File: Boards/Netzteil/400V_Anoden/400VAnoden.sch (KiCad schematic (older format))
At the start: 48 parts, among them P1 Drossel, P2 320V_AC, P3 Stabi, P4 133V_AC, P5 Stabi, P6 Trafo, P7 Trafo, P8 Relay, Q1 2SC2979

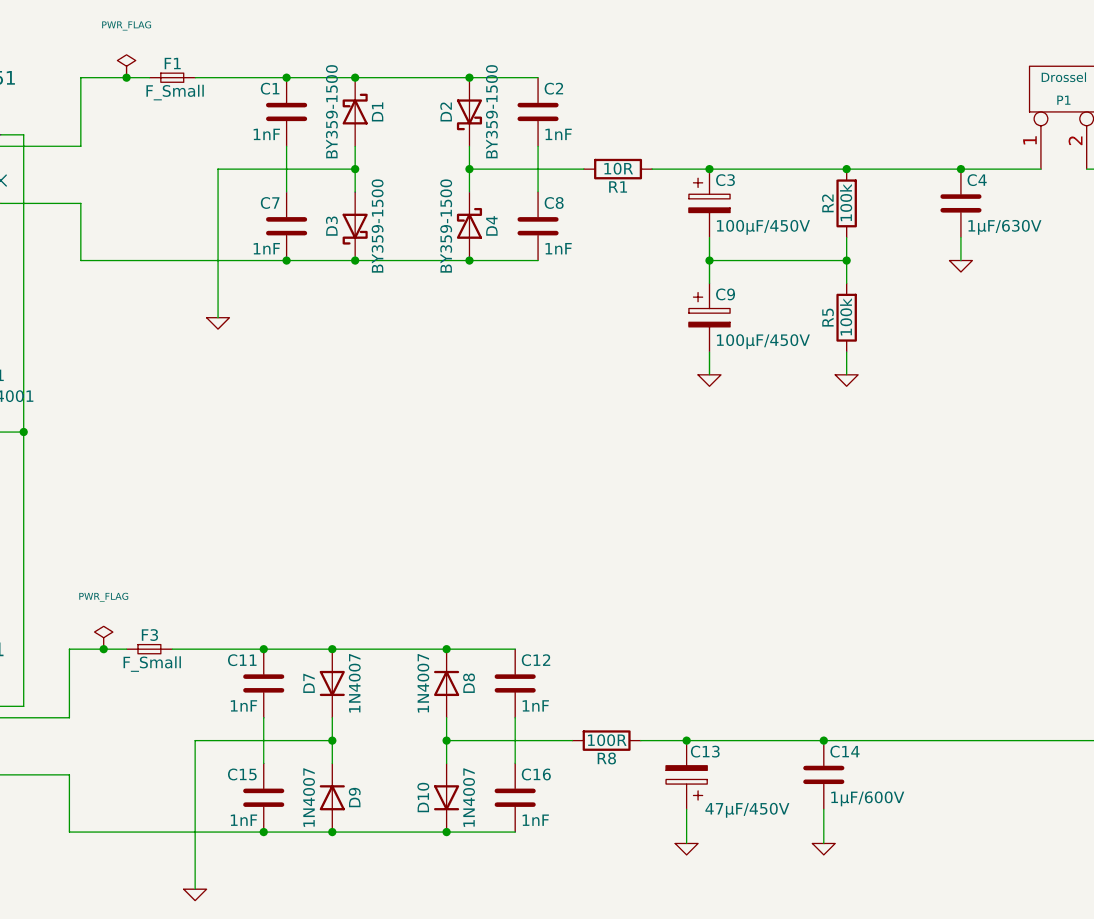
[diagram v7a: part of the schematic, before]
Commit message: 6,3V und 12V auf einer Platine zusammengefasst
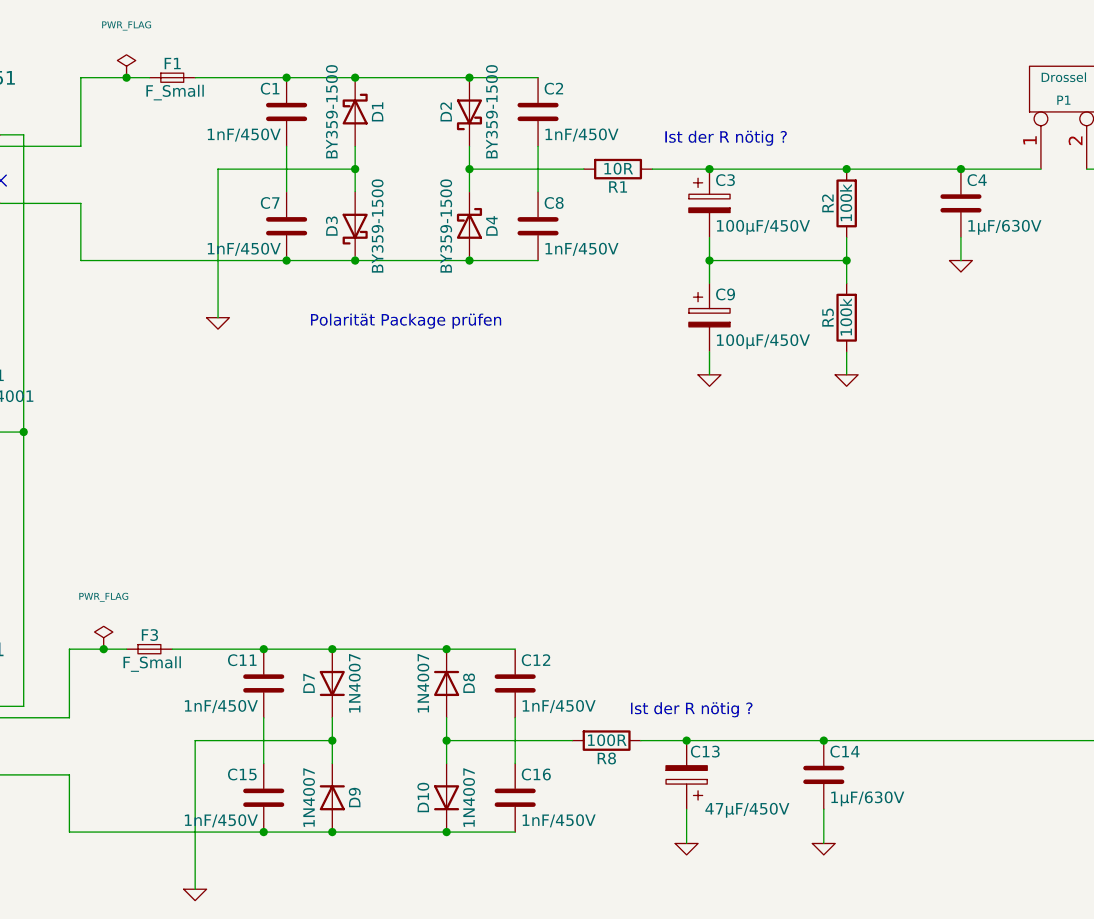
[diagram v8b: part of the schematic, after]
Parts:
- C1, C11, C12, C15, C16, C2, C7, C8: value 1nF -> 1nF/450V; footprint Capacitor_THT:C_Rect_L18.0mm_W5.0mm_P15.00mm_FKS3_FKP3 -> Capacitor_THT:C_Rect_L10.0mm_W4.0mm_P7.50mm_FKS3_FKP3
- C14: value 1µF/600V -> 1µF/630V; footprint Capacitor_THT:C_Rect_L41.5mm_W20.0mm_P37.50mm_MKS4 -> Capacitor_THT:C_Rect_L31.5mm_W11.0mm_P27.50mm_MKS4
- C3: footprint Capacitor_THT:CP_Radial_D22.0mm_P10.00mm_SnapIn -> Capacitor_THT:CP_Radial_D18.0mm_P7.50mm
- C4, C5: footprint Capacitor_THT:C_Rect_L41.5mm_W20.0mm_P37.50mm_MKS4 -> Capacitor_THT:C_Rect_L31.5mm_W11.0mm_P27.50mm_MKS4
- Q1: footprint Package_TO_SOT_THT:TO-220-3_Horizontal_TabDown -> Package_TO_SOT_THT:TO-218-3_Vertical
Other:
- note added: "Ist der R nötig ?"
- note added: "Polarität Package prüfen"
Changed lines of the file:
@@
 EESchema Schematic File Version 4
-LIBS:400VAnoden-cache
 EELAYER 30 0
 EELAYER END
@@
 F 0 "C3" H 5125 2750 50  0000 L CNN
 F 1 "100µF/450V" H 5125 2550 50  0000 L CNN
-F 2 "Capacitor_THT:CP_Radial_D22.0mm_P10.00mm_SnapIn" H 5138 2500 30  0001 C CNN
+F 2 "Capacitor_THT:CP_Radial_D18.0mm_P7.50mm" H 5138 2500 30  0001 C CNN
 F 3 "" H 5100 2650 60  0000 C CNN
 	1    5100 2650
@@
 F 0 "C4" H 6225 2750 50  0000 L CNN
 F 1 "1µF/630V" H 6225 2550 50  0000 L CNN
-F 2 "Capacitor_THT:C_Rect_L41.5mm_W20.0mm_P37.50mm_MKS4" H 6238 2500 30  0001 C CNN
+F 2 "Capacitor_THT:C_Rect_L31.5mm_W11.0mm_P27.50mm_MKS4" H 6238 2500 30  0001 C CNN
 F 3 "" H 6200 2650 60  0000 C CNN
 	1    6200 2650
@@
 F 0 "C5" H 7025 2750 50  0000 L CNN
 F 1 "1µF/630V" H 7025 2550 50  0000 L CNN
-F 2 "Capacitor_THT:C_Rect_L41.5mm_W20.0mm_P37.50mm_MKS4" H 7038 2500 30  0001 C CNN
+F 2 "Capacitor_THT:C_Rect_L31.5mm_W11.0mm_P27.50mm_MKS4" H 7038 2500 30  0001 C CNN
 F 3 "" H 7000 2650 60  0000 C CNN
 	1    7000 2650
@@
 F 0 "Q1" H 9450 2950 50  0000 R CNN
 F 1 "2SC2979" H 9750 2850 50  0000 R CNN
-F 2 "Package_TO_SOT_THT:TO-220-3_Horizontal_TabDown" H 9350 3000 29  0001 C CNN
+F 2 "Package_TO_SOT_THT:TO-218-3_Vertical" H 9350 3000 29  0001 C CNN
 F 3 "" H 9150 2900 60  0000 C CNN
 	1    9150 2900
@@
 P 5600 5150
 F 0 "C14" H 5625 5250 50  0000 L CNN
-F 1 "1µF/600V" H 5625 5050 50  0000 L CNN
-F 2 "Capacitor_THT:C_Rect_L41.5mm_W20.0mm_P37.50mm_MKS4" H 5638 5000 30  0001 C CNN
+F 1 "1µF/630V" H 5625 5050 50  0000 L CNN
+F 2 "Capacitor_THT:C_Rect_L31.5mm_W11.0mm_P27.50mm_MKS4" H 5638 5000 30  0001 C CNN
 F 3 "" H 5600 5150 60  0000 C CNN
 	1    5600 5150
@@
 P 3250 2250
 F 0 "C1" H 3275 2350 50  0000 L CNN
-F 1 "1nF" H 3275 2150 50  0000 L CNN
-F 2 "Capacitor_THT:C_Rect_L18.0mm_W5.0mm_P15.00mm_FKS3_FKP3" H 3288 2100 30  0001 C CNN
+F 1 "1nF/450V" H 3275 2150 50  0000 L CNN
+F 2 "Capacitor_THT:C_Rect_L10.0mm_W4.0mm_P7.50mm_FKS3_FKP3" H 3288 2100 30  0001 C CNN
 F 3 "" H 3250 2250 60  0000 C CNN
 	1    3250 2250
@@
 P 3250 2750
 F 0 "C7" H 3275 2850 50  0000 L CNN
-F 1 "1nF" H 3275 2650 50  0000 L CNN
-F 2 "Capacitor_THT:C_Rect_L18.0mm_W5.0mm_P15.00mm_FKS3_FKP3" H 3288 2600 30  0001 C CNN
+F 1 "1nF/450V" H 3275 2650 50  0000 L CNN
+F 2 "Capacitor_THT:C_Rect_L10.0mm_W4.0mm_P7.50mm_FKS3_FKP3" H 3288 2600 30  0001 C CNN
 F 3 "" H 3250 2750 60  0000 C CNN
 	1    3250 2750
@@
 P 4350 2250
 F 0 "C2" H 4375 2350 50  0000 L CNN
-F 1 "1nF" H 4375 2150 50  0000 L CNN
-F 2 "Capacitor_THT:C_Rect_L18.0mm_W5.0mm_P15.00mm_FKS3_FKP3" H 4388 2100 30  0001 C CNN
+F 1 "1nF/450V" H 4375 2150 50  0000 L CNN
+F 2 "Capacitor_THT:C_Rect_L10.0mm_W4.0mm_P7.50mm_FKS3_FKP3" H 4388 2100 30  0001 C CNN
 F 3 "" H 4350 2250 60  0000 C CNN
 	1    4350 2250
@@
 P 4350 2750
 F 0 "C8" H 4375 2850 50  0000 L CNN
-F 1 "1nF" H 4375 2650 50  0000 L CNN
-F 2 "Capacitor_THT:C_Rect_L18.0mm_W5.0mm_P15.00mm_FKS3_FKP3" H 4388 2600 30  0001 C CNN
+F 1 "1nF/450V" H 4375 2650 50  0000 L CNN
+F 2 "Capacitor_THT:C_Rect_L10.0mm_W4.0mm_P7.50mm_FKS3_FKP3" H 4388 2600 30  0001 C CNN
 F 3 "" H 4350 2750 60  0000 C CNN
 	1    4350 2750
@@
 P 3150 4750
 F 0 "C11" H 3175 4850 50  0000 L CNN
-F 1 "1nF" H 3175 4650 50  0000 L CNN
-F 2 "Capacitor_THT:C_Rect_L18.0mm_W5.0mm_P15.00mm_FKS3_FKP3" H 3188 4600 30  0001 C CNN
+F 1 "1nF/450V" H 3175 4650 50  0000 L CNN
+F 2 "Capacitor_THT:C_Rect_L10.0mm_W4.0mm_P7.50mm_FKS3_FKP3" H 3188 4600 30  0001 C CNN
 F 3 "" H 3150 4750 60  0000 C CNN
 	1    3150 4750
@@
 P 3150 5250
 F 0 "C15" H 3175 5350 50  0000 L CNN
-F 1 "1nF" H 3175 5150 50  0000 L CNN
-F 2 "Capacitor_THT:C_Rect_L18.0mm_W5.0mm_P15.00mm_FKS3_FKP3" H 3188 5100 30  0001 C CNN
+F 1 "1nF/450V" H 3175 5150 50  0000 L CNN
+F 2 "Capacitor_THT:C_Rect_L10.0mm_W4.0mm_P7.50mm_FKS3_FKP3" H 3188 5100 30  0001 C CNN
 F 3 "" H 3150 5250 60  0000 C CNN
 	1    3150 5250
@@
 P 4250 4750
 F 0 "C12" H 4275 4850 50  0000 L CNN
-F 1 "1nF" H 4275 4650 50  0000 L CNN
-F 2 "Capacitor_THT:C_Rect_L18.0mm_W5.0mm_P15.00mm_FKS3_FKP3" H 4288 4600 30  0001 C CNN
+F 1 "1nF/450V" H 4275 4650 50  0000 L CNN
+F 2 "Capacitor_THT:C_Rect_L10.0mm_W4.0mm_P7.50mm_FKS3_FKP3" H 4288 4600 30  0001 C CNN
 F 3 "" H 4250 4750 60  0000 C CNN
 	1    4250 4750
@@
 P 4250 5250
 F 0 "C16" H 4275 5350 50  0000 L CNN
-F 1 "1nF" H 4275 5150 50  0000 L CNN
-F 2 "Capacitor_THT:C_Rect_L18.0mm_W5.0mm_P15.00mm_FKS3_FKP3" H 4288 5100 30  0001 C CNN
+F 1 "1nF/450V" H 4275 5150 50  0000 L CNN
+F 2 "Capacitor_THT:C_Rect_L10.0mm_W4.0mm_P7.50mm_FKS3_FKP3" H 4288 5100 30  0001 C CNN
 F 3 "" H 4250 5250 60  0000 C CNN
 	1    4250 5250
@@
 Wire Wire Line
 	2300 4900 2300 4600
+Text Notes 4900 2400 0    50   ~ 0
+Ist der R nötig ?
+Text Notes 4750 4900 0    50   ~ 0
+Ist der R nötig ?
+Text Notes 3350 3200 0    50   ~ 0
+Polarität Package prüfen
 $EndSCHEMATC
